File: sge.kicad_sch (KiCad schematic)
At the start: 23 parts, among them IC6 315-5660

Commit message: Fill zones, DRC fixes.
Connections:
- net PC0: now reaches IC6.85 (PC0)
- net PC1: now reaches IC6.86 (PC1)
- net PC2: now reaches IC6.87 (PC2)
- net PC3: now reaches IC6.88 (PC3)
- net PC4: now reaches IC6.89 (PC4)
- net PC5: now reaches IC6.90 (PC5)
- net PC6: now reaches IC6.91 (PC6)
- no-connect marks 26 -> 19
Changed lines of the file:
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@@
   (no_connect (at 256.54 219.71))
   (no_connect (at 149.86 43.18))
-  (no_connect (at 303.53 43.18))
-  (no_connect (at 326.39 43.18))
   (no_connect (at 264.16 219.71))
-  (no_connect (at 307.34 43.18))
   (no_connect (at 339.09 43.18))
-  (no_connect (at 322.58 43.18))
   (no_connect (at 346.71 43.18))
   (no_connect (at 91.44 43.18))
   (no_connect (at 146.05 43.18))
-  (no_connect (at 311.15 43.18))
-  (no_connect (at 318.77 43.18))
   (no_connect (at 87.63 43.18))
-  (no_connect (at 314.96 43.18))
   (no_connect (at 227.33 43.18))
   (no_connect (at 252.73 219.71))
@@
     (stroke (width 0) (type default))
   )
+  (bus_entry (at 322.58 30.48) (size 2.54 -2.54)
+    (stroke (width 0) (type default))
+  )
   (bus_entry (at 111.76 233.68) (size 2.54 -2.54)
     (stroke (width 0) (type default))
@@
     (stroke (width 0) (type default))
   )
+  (bus_entry (at 303.53 30.48) (size 2.54 -2.54)
+    (stroke (width 0) (type default))
+  )
   (bus_entry (at 149.86 233.68) (size 2.54 -2.54)
     (stroke (width 0) (type default))
@@
     (stroke (width 0) (type default))
   )
+  (bus_entry (at 326.39 30.48) (size 2.54 -2.54)
+    (stroke (width 0) (type default))
+  )
+  (bus_entry (at 307.34 30.48) (size 2.54 -2.54)
+    (stroke (width 0) (type default))
+  )
   (bus_entry (at 119.38 233.68) (size 2.54 -2.54)
     (stroke (width 0) (type default))
@@
     (stroke (width 0) (type default))
   )
+  (bus_entry (at 318.77 30.48) (size 2.54 -2.54)
+    (stroke (width 0) (type default))
+  )
   (bus_entry (at 130.81 233.68) (size 2.54 -2.54)
     (stroke (width 0) (type default))
@@
     (stroke (width 0) (type default))
   )
+  (bus_entry (at 311.15 30.48) (size 2.54 -2.54)
+    (stroke (width 0) (type default))
+  )
   (bus_entry (at 153.67 233.68) (size 2.54 -2.54)
     (stroke (width 0) (type default))
   )
+  (bus_entry (at 314.96 30.48) (size 2.54 -2.54)
+    (stroke (width 0) (type default))
+  )
   (bus_entry (at 375.92 167.64) (size 2.54 2.54)
     (stroke (width 0) (type default))
@@
     (stroke (width 0) (type default))
   )
+  (wire (pts (xy 326.39 30.48) (xy 326.39 43.18))
+    (stroke (width 0) (type default))
+  )
   (wire (pts (xy 364.49 60.96) (xy 375.92 60.96))
     (stroke (width 0) (type default))
@@
     (stroke (width 0) (type default))
   )
+  (wire (pts (xy 318.77 30.48) (xy 318.77 43.18))
+    (stroke (width 0) (type default))
+  )
   (wire (pts (xy 264.16 228.6) (xy 264.16 231.775))
     (stroke (width 0) (type default))
@@
     (stroke (width 0) (type default))
   )
+  (bus (pts (xy 306.07 27.94) (xy 309.88 27.94))
+    (stroke (width 0) (type default))
+  )
   (wire (pts (xy 228.6 219.71) (xy 228.6 234.95))
     (stroke (width 0) (type default))
@@
     (stroke (width 0) (type default))
   )
+  (bus (pts (xy 321.31 27.94) (xy 325.12 27.94))
+    (stroke (width 0) (type default))
+  )
   (wire (pts (xy 275.59 231.775) (xy 275.59 219.71))
     (stroke (width 0) (type default))
@@
     (stroke (width 0) (type default))
   )
+  (bus (pts (xy 328.93 27.94) (xy 332.74 27.94))
+    (stroke (width 0) (type default))
+  )
   (wire (pts (xy 186.69 41.91) (xy 186.69 43.18))
     (stroke (width 0) (type default))
@@
     (stroke (width 0) (type default))
   )
+  (wire (pts (xy 322.58 30.48) (xy 322.58 43.18))
+    (stroke (width 0) (type default))
+  )
   (wire (pts (xy 50.8 148.59) (xy 62.23 148.59))
     (stroke (width 0) (type default))
@@
     (stroke (width 0) (type default))
   )
+  (wire (pts (xy 311.15 30.48) (xy 311.15 43.18))
+    (stroke (width 0) (type default))
+  )
   (wire (pts (xy 50.8 76.2) (xy 62.23 76.2))
     (stroke (width 0) (type default))
@@
     (stroke (width 0) (type default))
   )
+  (wire (pts (xy 303.53 30.48) (xy 303.53 43.18))
+    (stroke (width 0) (type default))
+  )
   (wire (pts (xy 50.8 194.31) (xy 62.23 194.31))
     (stroke (width 0) (type default))
@@
     (stroke (width 0) (type default))
   )
+  (bus (pts (xy 309.88 27.94) (xy 313.69 27.94))
+    (stroke (width 0) (type default))
+  )
   (wire (pts (xy 273.05 231.775) (xy 270.51 231.775))
     (stroke (width 0) (type default))
@@
     (stroke (width 0) (type default))
   )
+  (bus (pts (xy 317.5 27.94) (xy 321.31 27.94))
+    (stroke (width 0) (type default))
+  )
   (wire (pts (xy 234.95 251.46) (xy 234.95 254.635))
     (stroke (width 0) (type default))
@@
     (stroke (width 0) (type default))
   )
+  (wire (pts (xy 314.96 30.48) (xy 314.96 43.18))
+    (stroke (width 0) (type default))
+  )
   (wire (pts (xy 364.49 163.83) (xy 375.92 163.83))
     (stroke (width 0) (type default))
@@
     (stroke (width 0) (type default))
   )
+  (bus (pts (xy 328.93 27.94) (xy 325.12 27.94))
+    (stroke (width 0) (type default))
+  )
   (wire (pts (xy 50.8 156.21) (xy 62.23 156.21))
     (stroke (width 0) (type default))
@@
     (stroke (width 0) (type default))
   )
+  (wire (pts (xy 307.34 30.48) (xy 307.34 43.18))
+    (stroke (width 0) (type default))
+  )
   (wire (pts (xy 261.62 254.635) (xy 272.415 254.635))
     (stroke (width 0) (type default))
@@
     (stroke (width 0) (type default))
   )
+  (bus (pts (xy 313.69 27.94) (xy 317.5 27.94))
+    (stroke (width 0) (type default))
+  )
   (wire (pts (xy 281.94 26.67) (xy 281.94 43.18))
     (stroke (width 0) (type default))
@@
     (effects (font (size 1.27 1.27)) (justify left bottom))
   )
+  (label "PC6" (at 326.39 38.1 90) (fields_autoplaced)
+    (effects (font (size 1.27 1.27)) (justify left bottom))
+  )
   (label "SD6" (at 201.93 31.75 90) (fields_autoplaced)
     (effects (font (size 1.27 1.27)) (justify left bottom))
@@
     (effects (font (size 1.27 1.27)) (justify right bottom))
   )
+  (label "PC3" (at 314.96 38.1 90) (fields_autoplaced)
+    (effects (font (size 1.27 1.27)) (justify left bottom))
+  )
   (label "PB6" (at 297.18 38.1 90) (fields_autoplaced)
     (effects (font (size 1.27 1.27)) (justify left bottom))
@@
     (effects (font (size 1.27 1.27)) (justify right bottom))
   )
+  (label "PC2" (at 311.15 38.1 90) (fields_autoplaced)
+    (effects (font (size 1.27 1.27)) (justify left bottom))
+  )
   (label "VD14" (at 224.79 222.885 270) (fields_autoplaced)
     (effects (font (size 1.27 1.27)) (justify right bottom))
@@
     (effects (font (size 1.27 1.27)) (justify left bottom))
   )
+  (label "PC1" (at 307.34 38.1 90) (fields_autoplaced)
+    (effects (font (size 1.27 1.27)) (justify left bottom))
+  )
   (label "VA4" (at 91.44 222.25 270) (fields_autoplaced)
     (effects (font (size 1.27 1.27)) (justify right bottom))
@@
     (effects (font (size 1.27 1.27)) (justify left bottom))
   )
+  (label "PC4" (at 318.77 38.1 90) (fields_autoplaced)
+    (effects (font (size 1.27 1.27)) (justify left bottom))
+  )
   (label "AD4" (at 128.27 31.75 90) (fields_autoplaced)
     (effects (font (size 1.27 1.27)) (justify left bottom))
@@
     (effects (font (size 1.27 1.27)) (justify right bottom))
   )
+  (label "PC5" (at 322.58 38.1 90) (fields_autoplaced)
+    (effects (font (size 1.27 1.27)) (justify left bottom))
+  )
   (label "ZD6" (at 367.665 118.11 0) (fields_autoplaced)
     (effects (font (size 1.27 1.27)) (justify left bottom))
@@
   )
   (label "PB2" (at 281.94 38.1 90) (fields_autoplaced)
+    (effects (font (size 1.27 1.27)) (justify left bottom))
+  )
+  (label "PC0" (at 303.53 38.1 90) (fields_autoplaced)
     (effects (font (size 1.27 1.27)) (justify left bottom))
   )
@@
     )
   )
+  (global_label "PC[0..6]" (shape bidirectional) (at 332.74 27.94 0) (fields_autoplaced)
+    (effects (font (size 1.27 1.27)) (justify left))
+    (property "Intersheetrefs" "${INTERSHEET_REFS}" (at 344.6985 27.94 0)
+      (effects (font (size 1.27 1.27)) (justify left) hide)
+    )
+  )

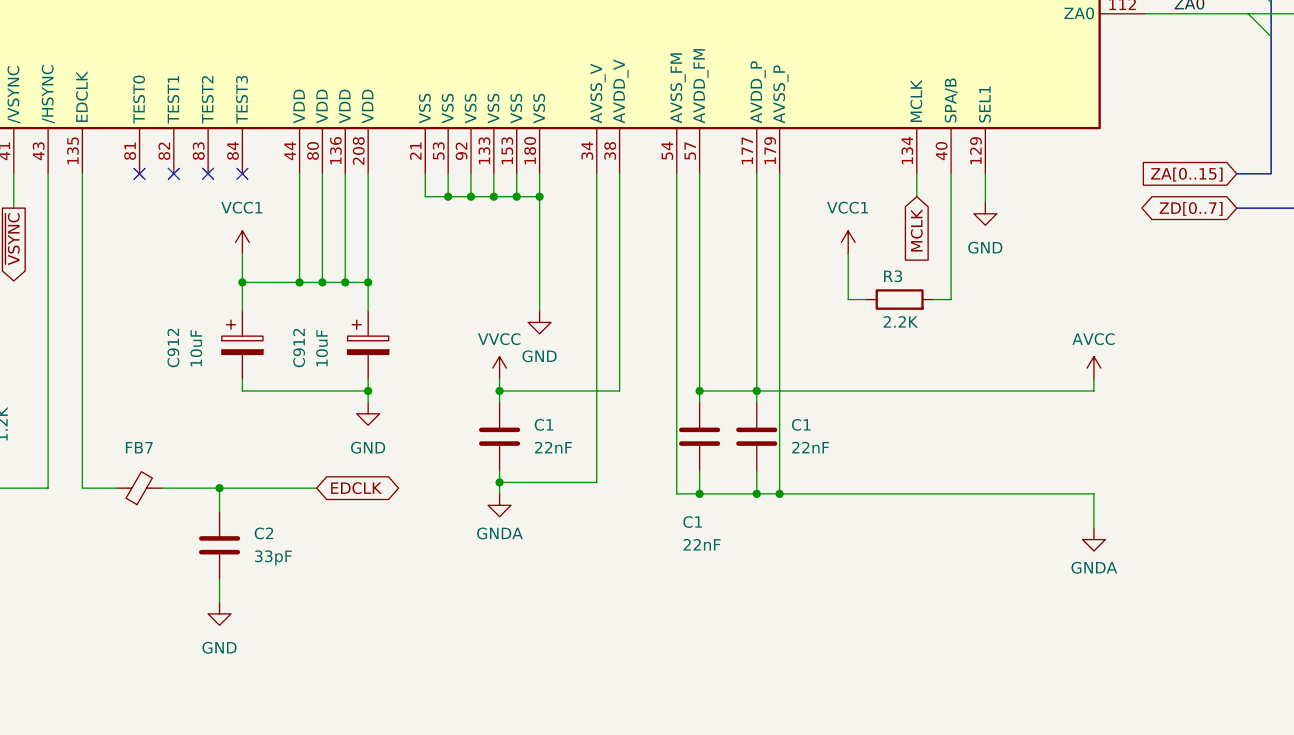
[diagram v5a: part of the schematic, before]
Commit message: SMS compatibility fixes.
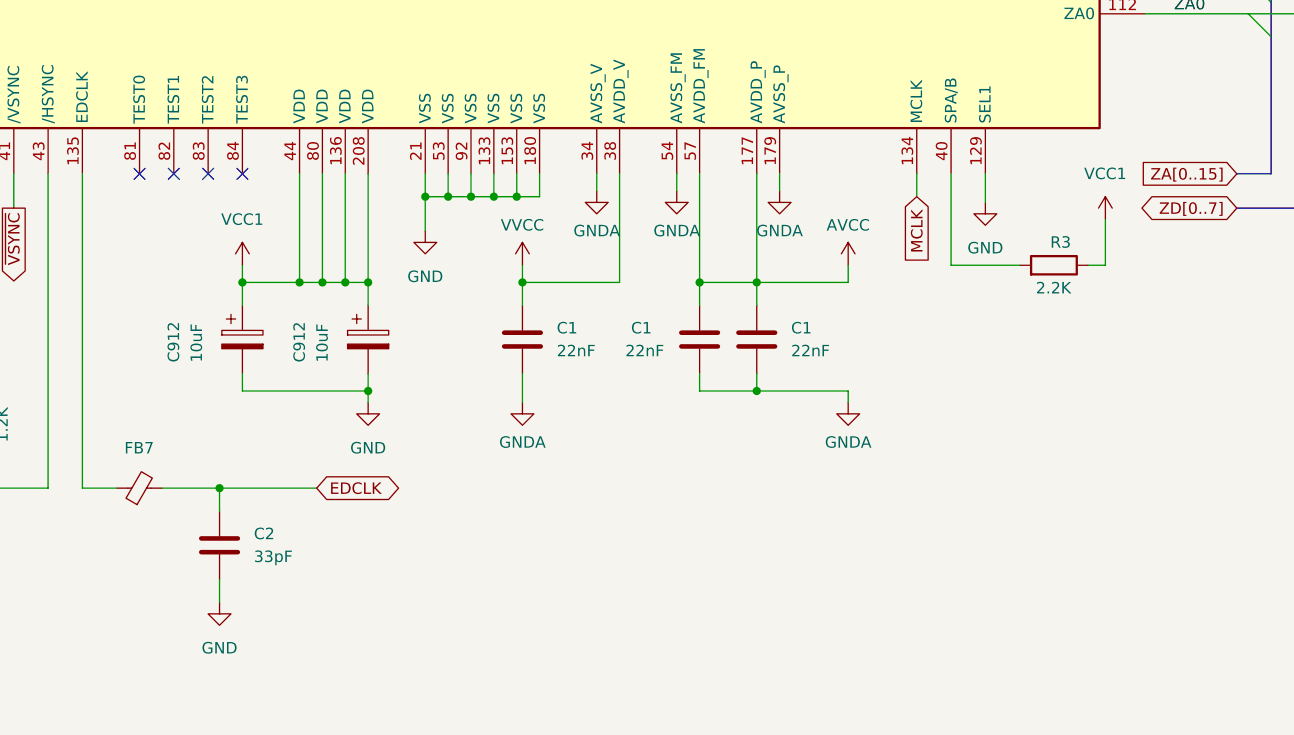
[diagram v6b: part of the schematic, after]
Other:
- moved on the sheet: C1, C912, R3

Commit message: Misc. tweaks/improvements.
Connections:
- net VCC1: now also RN1.1 (R1.1), RN1.2 (R2.1), RN1.3 (R3.1), RN1.4 (R4.1); no longer RN1.5 (R4.2), RN1.6 (R3.2), RN1.7 (R2.2), RN1.8 (R1.2)
- net ~{BGAK}: now also RN1.6 (R3.2); no longer RN1.3 (R3.1)
- net ~{BR}: now also RN1.5 (R4.2); no longer RN1.4 (R4.1)
- net ~{IPL1}: now also RN1.7 (R2.2); no longer RN1.2 (R2.1)
- net ~{IPL2}: now also RN1.8 (R1.2); no longer RN1.1 (R1.1)
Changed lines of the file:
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@@
     (title "SGE (MD Custom ASIC)")
     (date "2023-11-29")
-    (rev "1.0")
+    (rev "1.1")
     (company "By Cosam")
     (comment 1 "Neptune")
@@
     )
   )
-  (symbol (lib_id "Device:R_Pack04") (at 127 256.54 0) (unit 1)
-    (in_bom yes) (on_board yes) (dnp no) (fields_autoplaced)
-    (property "Reference" "RN1" (at 132.08 255.27 0)
-      (effects (font (size 1.27 1.27)) (justify left))
+  (symbol (lib_id "Device:R_Pack04") (at 127 256.54 0) (mirror x) (unit 1)
+    (in_bom yes) (on_board yes) (dnp no)
+    (property "Reference" "RN1" (at 118.745 255.27 0)
+      (effects (font (size 1.27 1.27)) (justify right))
     )
-    (property "Value" "4x2.2K" (at 132.08 257.81 0)
-      (effects (font (size 1.27 1.27)) (justify left))
+    (property "Value" "4x2.2K" (at 118.745 257.81 0)
+      (effects (font (size 1.27 1.27)) (justify right))
     )
     (property "Footprint" "Resistor_SMD:R_Array_Convex_4x0603" (at 133.985 256.54 90)

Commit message: General tweaks, add some DigiKey part numbers.
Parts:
- R3: DigiKey (none) -> P2.20KCCT-ND
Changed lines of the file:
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@@
+      (effects (font (size 1.27 1.27)) hide)
+    )
+    (property "DigiKey" "" (at 113.03 38.1 0)
       (effects (font (size 1.27 1.27)) hide)
     )
@@
     )
     (property "Datasheet" "" (at 243.84 287.02 0)
+      (effects (font (size 1.27 1.27)) hide)
+    )
+    (property "DigiKey" "" (at 213.36 130.81 0)
       (effects (font (size 1.27 1.27)) hide)
     )
@@
       (effects (font (size 1.27 1.27)) hide)
     )
+    (property "DigiKey" "P2.20KCCT-ND" (at 145.415 256.54 0)
+      (effects (font (size 1.27 1.27)) hide)
+    )
     (pin "1")
     (pin "2")
@@
       (effects (font (size 1.27 1.27)) hide)
     )
+    (property "DigiKey" "" (at 99.06 38.1 0)
+      (effects (font (size 1.27 1.27)) hide)
+    )
     (pin "1")
     (pin "8")
@@
       (effects (font (size 1.27 1.27)) hide)
     )
+    (property "DigiKey" "" (at 124.46 38.1 0)
+      (effects (font (size 1.27 1.27)) hide)
+    )
     (pin "1")
     (pin "8")
@@
       (effects (font (size 1.27 1.27)) hide)
     )
+    (property "DigiKey" "" (at 116.84 38.1 0)
+      (effects (font (size 1.27 1.27)) hide)
+    )
     (pin "1")
     (pin "8")
@@
     )
     (property "Datasheet" "~" (at 264.16 238.125 0)
+      (effects (font (size 1.27 1.27)) hide)
+    )
+    (property "DigiKey" "" (at 264.16 238.125 0)
       (effects (font (size 1.27 1.27)) hide)
     )
@@
       (effects (font (size 1.27 1.27)) hide)
     )
+    (property "DigiKey" "" (at 198.12 38.1 0)
+      (effects (font (size 1.27 1.27)) hide)
+    )
     (pin "1")
     (pin "8")
@@
       (effects (font (size 1.27 1.27)) hide)
     )
+    (property "DigiKey" "" (at 261.62 260.985 0)
+      (effects (font (size 1.27 1.27)) hide)
+    )
     (pin "1")
     (pin "2")
@@
       (effects (font (size 1.27 1.27)) hide)
     )
+    (property "DigiKey" "" (at 106.68 38.1 0)
+      (effects (font (size 1.27 1.27)) hide)
+    )
     (pin "1")
     (pin "4")
@@
       (effects (font (size 1.27 1.27)) hide)
     )
+    (property "DigiKey" "P2.20KCCT-ND" (at 390.525 57.785 0)
+      (effects (font (size 1.27 1.27)) hide)
+    )
     (pin "1")
     (pin "2")
@@
       (effects (font (size 1.27 1.27)) hide)
     )
+    (property "DigiKey" "" (at 30.48 174.625 0)
+      (effects (font (size 1.27 1.27)) hide)
+    )
     (pin "1")
     (pin "2")
@@
       (effects (font (size 1.27 1.27)) hide)
     )
+    (property "DigiKey" "" (at 170.18 265.43 0)
+      (effects (font (size 1.27 1.27)) hide)
+    )
     (pin "1")
     (pin "2")
@@
       (effects (font (size 1.27 1.27)) hide)
     )
+    (property "DigiKey" "" (at 295.275 238.125 0)
+      (effects (font (size 1.27 1.27)) hide)
+    )
     (pin "1")
     (pin "2")
@@
       (effects (font (size 1.27 1.27)) hide)
     )
+    (property "DigiKey" "" (at 135.89 38.1 0)
+      (effects (font (size 1.27 1.27)) hide)
+    )
     (pin "1")
     (pin "8")
@@
       (effects (font (size 1.27 1.27)) hide)
     )
+    (property "DigiKey" "" (at 83.82 38.1 0)
+      (effects (font (size 1.27 1.27)) hide)
+    )
     (pin "1")
     (pin "4")
@@
     )
     (property "Datasheet" "~" (at 120.65 38.1 0)
+      (effects (font (size 1.27 1.27)) hide)
+    )
+    (property "DigiKey" "" (at 120.65 38.1 0)
       (effects (font (size 1.27 1.27)) hide)
     )
@@
       (effects (font (size 1.27 1.27)) hide)
     )
+    (property "DigiKey" "" (at 179.07 38.1 0)
+      (effects (font (size 1.27 1.27)) hide)
+    )
     (pin "1")
     (pin "8")
@@
       (effects (font (size 1.27 1.27)) hide)
     )
+    (property "DigiKey" "P2.20KCCT-ND" (at 354.33 229.87 0)
+      (effects (font (size 1.27 1.27)) hide)
+    )
     (pin "1")
     (pin "2")
@@
       (effects (font (size 1.27 1.27)) hide)
     )
+    (property "DigiKey" "" (at 132.08 38.1 0)
+      (effects (font (size 1.27 1.27)) hide)
+    )
     (pin "1")
     (pin "8")
@@
       (effects (font (size 1.27 1.27)) hide)
     )
+    (property "DigiKey" "" (at 127 256.54 0)
+      (effects (font (size 1.27 1.27)) hide)
+    )
     (pin "1")
     (pin "2")
@@
       (effects (font (size 1.27 1.27)) hide)
     )
+    (property "DigiKey" "" (at 201.93 38.1 0)
+      (effects (font (size 1.27 1.27)) hide)
+    )
     (pin "1")
     (pin "8")
@@
     )
     (property "Datasheet" "~" (at 321.31 238.125 0)
+      (effects (font (size 1.27 1.27)) hide)
+    )
+    (property "DigiKey" "" (at 321.31 238.125 0)
       (effects (font (size 1.27 1.27)) hide)
     )
@@
       (effects (font (size 1.27 1.27)) hide)
     )
+    (property "DigiKey" "" (at 194.31 38.1 0)
+      (effects (font (size 1.27 1.27)) hide)
+    )
     (pin "1")
     (pin "8")
@@
       (effects (font (size 1.27 1.27)) hide)
     )
+    (property "DigiKey" "" (at 128.27 38.1 0)
+      (effects (font (size 1.27 1.27)) hide)
+    )
     (pin "1")
     (pin "8")
@@
     )
     (property "Datasheet" "~" (at 102.87 38.1 0)
+      (effects (font (size 1.27 1.27)) hide)
+    )
+    (property "DigiKey" "" (at 102.87 38.1 0)
       (effects (font (size 1.27 1.27)) hide)
     )
@@
       (effects (font (size 1.27 1.27)) hide)
     )
+    (property "DigiKey" "" (at 390.525 195.58 0)
+      (effects (font (size 1.27 1.27)) hide)
+    )
     (pin "1")
     (pin "2")
@@
       (effects (font (size 1.27 1.27)) hide)
     )
+    (property "DigiKey" "" (at 314.96 238.125 0)
+      (effects (font (size 1.27 1.27)) hide)
+    )
     (pin "1")
     (pin "2")
@@
       (effects (font (size 1.27 1.27)) hide)
     )
+    (property "DigiKey" "" (at 80.01 38.1 0)
+      (effects (font (size 1.27 1.27)) hide)
+    )
     (pin "1")
     (pin "8")
@@
     )
     (property "Datasheet" "~" (at 252.73 254.635 0)
+      (effects (font (size 1.27 1.27)) hide)
+    )
+    (property "DigiKey" "" (at 252.73 254.635 0)
       (effects (font (size 1.27 1.27)) hide)
     )
@@
       (effects (font (size 1.27 1.27)) hide)
     )
+    (property "DigiKey" "" (at 190.5 38.1 0)
+      (effects (font (size 1.27 1.27)) hide)
+    )
     (pin "1")
     (pin "8")
@@
     )
     (property "Datasheet" "~" (at 139.7 38.1 0)
+      (effects (font (size 1.27 1.27)) hide)
+    )
+    (property "DigiKey" "" (at 139.7 38.1 0)
       (effects (font (size 1.27 1.27)) hide)
     )
@@
       (effects (font (size 1.27 1.27)) hide)
     )
+    (property "DigiKey" "" (at 234.95 247.65 0)
+      (effects (font (size 1.27 1.27)) hide)
+    )
     (pin "1")
     (pin "2")
@@
       (effects (font (size 1.27 1.27)) hide)
     )
+    (property "DigiKey" "" (at 278.13 238.125 0)
+      (effects (font (size 1.27 1.27)) hide)
+    )
     (pin "1")
     (pin "2")
@@
       (effects (font (size 1.27 1.27)) hide)
     )
+    (property "DigiKey" "" (at 205.74 38.1 0)
+      (effects (font (size 1.27 1.27)) hide)
+    )
     (pin "1")
     (pin "8")
@@
       (effects (font (size 1.27 1.27)) hide)
     )
+    (property "DigiKey" "" (at 95.25 38.1 0)
+      (effects (font (size 1.27 1.27)) hide)
+    )
     (pin "1")
     (pin "8")
@@
     )
     (property "Datasheet" "~" (at 31.115 71.755 0)
+      (effects (font (size 1.27 1.27)) hide)
+    )
+    (property "DigiKey" "" (at 31.115 71.755 0)
       (effects (font (size 1.27 1.27)) hide)
     )
@@
       (effects (font (size 1.27 1.27)) hide)
     )
+    (property "DigiKey" "" (at 186.69 38.1 0)
+      (effects (font (size 1.27 1.27)) hide)
+    )
     (pin "1")
     (pin "8")
@@
       (effects (font (size 1.27 1.27)) hide)
     )
+    (property "DigiKey" "" (at 182.88 38.1 0)
+      (effects (font (size 1.27 1.27)) hide)
+    )
